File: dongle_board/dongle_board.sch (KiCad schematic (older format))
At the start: 11 parts

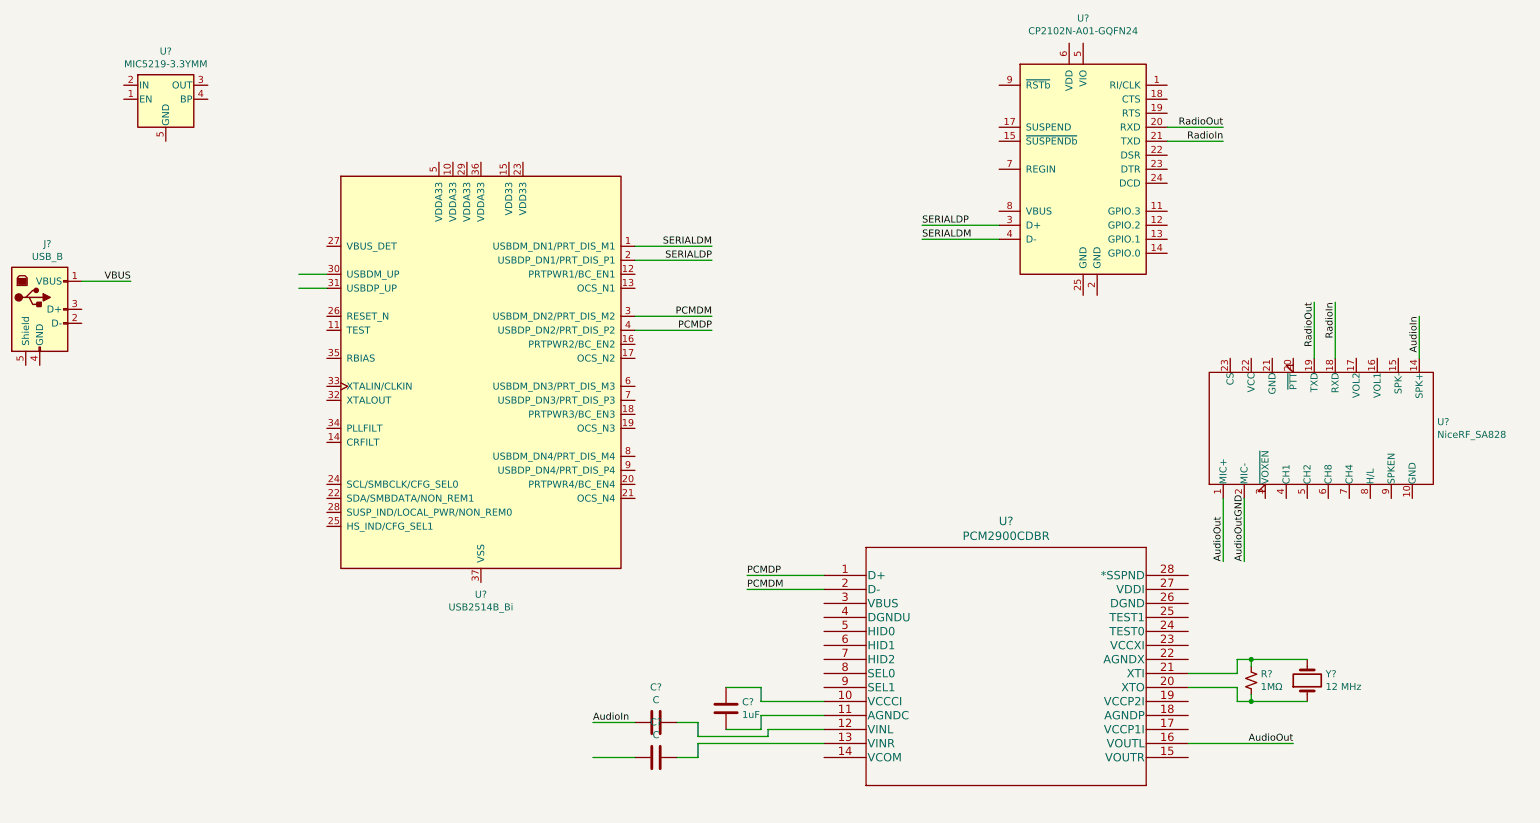
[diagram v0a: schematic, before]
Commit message: Added a bunch of wiring for the codec.
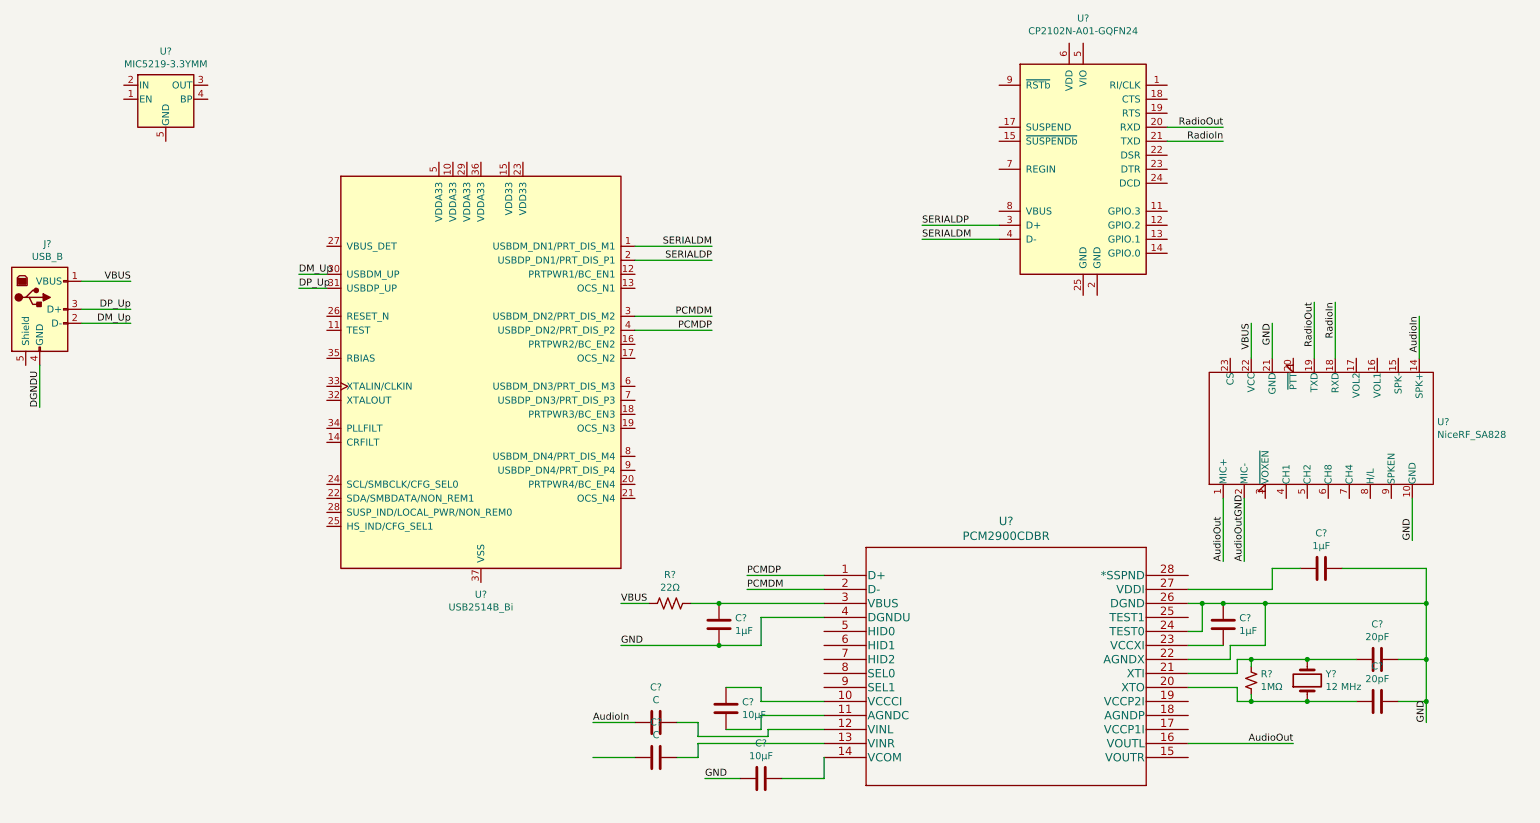
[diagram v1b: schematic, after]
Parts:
- added C? (x3): 1μF, symbol Device:C
- added C? (x2): 20pF, symbol Device:C
- added C?: 10μF, symbol Device:C
- added R?: 22Ω, symbol Device:R_US
- C?: value 1uF -> 10μF
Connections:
- net labels added: DGNDU, DM_Up, DP_Up, GND
- wire segments 45 -> 84
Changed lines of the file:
@@
 P 5750 5550
 F 0 "C?" H 5865 5596 50  0000 L CNN
-F 1 "1uF" H 5865 5505 50  0000 L CNN
+F 1 "10μF" H 5865 5505 50  0000 L CNN
 F 2 "" H 5788 5400 50  0001 C CNN
 F 3 "~" H 5750 5550 50  0001 C CNN
@@
 Wire Wire Line
 	2900 2550 2700 2550
+$Comp
+L Device:R_US R?
+U 1 1 5D57F03F
+P 5350 4800
+F 0 "R?" V 5145 4800 50  0000 C CNN
+F 1 "22Ω" V 5236 4800 50  0000 C CNN
+F 2 "" V 5390 4790 50  0001 C CNN
+F 3 "~" H 5350 4800 50  0001 C CNN
+	1    5350 4800
+	0    1    1    0
+$EndComp
+Wire Wire Line
+	5500 4800 5700 4800
+$Comp
+L Device:C C?
+U 1 1 5D589C1D
+P 5700 4950
+F 0 "C?" H 5815 4996 50  0000 L CNN
+F 1 "1μF" H 5815 4905 50  0000 L CNN
+F 2 "" H 5738 4800 50  0001 C CNN
+F 3 "~" H 5700 4950 50  0001 C CNN
+	1    5700 4950
+	1    0    0    -1
+$EndComp
+Connection ~ 5700 4800
+Wire Wire Line
+	5700 4800 6450 4800
+Wire Wire Line
+	6450 4900 6000 4900
+Wire Wire Line
+	6000 4900 6000 5100
+Wire Wire Line
+	6000 5100 5700 5100
+Wire Wire Line
+	5700 5100 5000 5100
+Connection ~ 5700 5100
+Wire Wire Line
+	5200 4800 5000 4800
+Text Label 5000 4800 0    50   ~ 0
+VBUS
+Wire Wire Line
+	850  3100 850  3400
+Text Label 850  3400 1    50   ~ 0
+DGNDU
+Wire Wire Line
+	1150 2700 1500 2700
+Wire Wire Line
+	1150 2800 1500 2800
+Text Label 1500 2700 2    50   ~ 0
+DP_Up
+Text Label 1500 2800 2    50   ~ 0
+DM_Up
+Text Label 2700 2450 0    50   ~ 0
+DM_Up
+Text Label 2700 2550 0    50   ~ 0
+DP_Up
+Wire Wire Line
+	10650 4050 10650 4350
+Text Label 10650 4350 1    50   ~ 0
+GND
+Wire Wire Line
+	9650 3050 9650 2800
+Text Label 9650 2800 3    50   ~ 0
+GND
+Wire Wire Line
+	9500 3050 9500 2800
+Text Label 9500 2800 3    50   ~ 0
+VBUS
+Wire Wire Line
+	9900 5200 10250 5200
+Connection ~ 9900 5200
+Wire Wire Line
+	9900 5500 10250 5500
+Connection ~ 9900 5500
+$Comp
+L Device:C C?
+U 1 1 5D5B9188
+P 10400 5200
+F 0 "C?" V 10148 5200 50  0000 C CNN
+F 1 "20pF" V 10239 5200 50  0000 C CNN
+F 2 "" H 10438 5050 50  0001 C CNN
+F 3 "~" H 10400 5200 50  0001 C CNN
+	1    10400 5200
+	0    1    1    0
+$EndComp
+$Comp
+L Device:C C?
+U 1 1 5D5B979E
+P 10400 5500
+F 0 "C?" V 10148 5500 50  0000 C CNN
+F 1 "20pF" V 10239 5500 50  0000 C CNN
+F 2 "" H 10438 5350 50  0001 C CNN
+F 3 "~" H 10400 5500 50  0001 C CNN
+	1    10400 5500
+	0    1    1    0
+$EndComp
+Wire Wire Line
+	10550 5200 10750 5200
+Wire Wire Line
+	10550 5500 10750 5500
+Wire Wire Line
+	10750 5500 10750 5650
+Wire Wire Line
+	10750 5200 10750 5500
+Connection ~ 10750 5500
+Text Label 10750 5650 1    50   ~ 0
+GND
+Connection ~ 10750 5200
+Wire Wire Line
+	10750 4800 10750 5200
+$Comp
+L Device:C C?
+U 1 1 5D5D03B6
+P 9300 4950
+F 0 "C?" H 9415 4996 50  0000 L CNN
+F 1 "1μF" H 9415 4905 50  0000 L CNN
+F 2 "" H 9338 4800 50  0001 C CNN
+F 3 "~" H 9300 4950 50  0001 C CNN
+	1    9300 4950
+	1    0    0    -1
+$EndComp
+Wire Wire Line
+	9050 5200 9350 5200
+Wire Wire Line
+	9350 5200 9350 5100
+Wire Wire Line
+	9350 5100 9600 5100
+Wire Wire Line
+	9600 5100 9600 4800
+Connection ~ 9600 4800
+Wire Wire Line
+	9600 4800 10750 4800
+Connection ~ 9300 4800
+Wire Wire Line
+	9300 4800 9600 4800
+Wire Wire Line
+	9050 4800 9150 4800
+Wire Wire Line
+	9050 5100 9300 5100
+Wire Wire Line
+	9050 5000 9150 5000
+Wire Wire Line
+	9150 5000 9150 4800
+Connection ~ 9150 4800
+Wire Wire Line
+	9150 4800 9300 4800
+Wire Wire Line
+	9050 4700 9650 4700
+Wire Wire Line
+	9650 4700 9650 4550
+Wire Wire Line
+	9650 4550 9850 4550
+$Comp
+L Device:C C?
+U 1 1 5D5EA132
+P 10000 4550
+F 0 "C?" V 9748 4550 50  0000 C CNN
+F 1 "1μF" V 9839 4550 50  0000 C CNN
+F 2 "" H 10038 4400 50  0001 C CNN
+F 3 "~" H 10000 4550 50  0001 C CNN
+	1    10000 4550
+	0    1    1    0
+$EndComp
+Wire Wire Line
+	10150 4550 10750 4550
+Wire Wire Line
+	10750 4550 10750 4800
+Connection ~ 10750 4800
+Wire Wire Line
+	6450 5900 6450 6050
+Wire Wire Line
+	6450 6050 6150 6050
+$Comp
+L Device:C C?
+U 1 1 5D5F12A8
+P 6000 6050
+F 0 "C?" V 5748 6050 50  0000 C CNN
+F 1 "10μF" V 5839 6050 50  0000 C CNN
+F 2 "" H 6038 5900 50  0001 C CNN
+F 3 "~" H 6000 6050 50  0001 C CNN
+	1    6000 6050
+	0    1    1    0
+$EndComp
+Wire Wire Line
+	5850 6050 5600 6050
+Text Label 5600 6050 0    50   ~ 0
+GND
+Text Label 5000 5100 0    50   ~ 0
+GND
 $EndSCHEMATC

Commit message: Added more connections.
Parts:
- added C? (x2): 1μF, symbol Device:C
- added R?: 1500Ω, symbol Device:R_Small_US
- added R? (x2): 22Ω, symbol Device:R_Small_US
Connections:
- net AudioOutGND is gone; now on net GND: U?.2 (MIC-)
- net DGNDU is gone; now on net GND: J?.4 (GND)
- net GND: now also C?.2, U?.11 (AGNDC), U?.18 (AGNDP), C?.1, C?.1
- net PCMDM: now also R?.2; no longer U?.2 (D-)
- net PCMDP: now also R?.2, R?.2; no longer U?.1 (D+)
- net at U?.17 (VCCP1I): now also C?.2
- net at U?.19 (VCCP2I): now also C?.2
- net V_Digital: now reaches C?.2, U?.27 (VDDI)
- net V_Digital: now also U?.8 (SEL0), U?.9 (SEL1), R?.1
- new net: R?.1, U?.1 (D+)
- new net: R?.1, U?.2 (D-)
- no-connect marks 0 -> 1
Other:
- moved on the sheet: C?, R?, U?, Y?

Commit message: Some updates!
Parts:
- added R?: 22.1kΩ, symbol Device:R_Small_US
- added R?: 47.5kΩ, symbol Device:R_Small_US
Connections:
- net GND: now also R?.2
- net VBUS: now also R?.1
- net at U?.8 (VBUS): now also R?.1, R?.2
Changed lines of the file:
@@
 Wire Wire Line
 	6000 4700 6450 4700
+Wire Wire Line
+	7700 2000 6850 2000
+$Comp
+L Device:R_Small_US R?
+U 1 1 5D62AB75
+P 6850 1900
+F 0 "R?" H 6918 1946 50  0000 L CNN
+F 1 "22.1kΩ" H 6918 1855 50  0000 L CNN
+F 2 "" H 6850 1900 50  0001 C CNN
+F 3 "~" H 6850 1900 50  0001 C CNN
+	1    6850 1900
+	1    0    0    -1
+$EndComp
+$Comp
+L Device:R_Small_US R?
+U 1 1 5D62C09F
+P 6850 2100
+F 0 "R?" H 6918 2146 50  0000 L CNN
+F 1 "47.5kΩ" H 6918 2055 50  0000 L CNN
+F 2 "" H 6850 2100 50  0001 C CNN
+F 3 "~" H 6850 2100 50  0001 C CNN
+	1    6850 2100
+	1    0    0    -1
+$EndComp
+Connection ~ 6850 2000
+Wire Wire Line
+	6850 1800 6850 1600
+Wire Wire Line
+	6850 2200 6850 2350
+Text Label 6850 2350 1    50   ~ 0
+GND
+Text Label 6850 1600 3    50   ~ 0
+VBUS
 $EndSCHEMATC
